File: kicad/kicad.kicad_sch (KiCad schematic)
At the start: 4 parts, among them SW1 SW_Push, U1 nice_nano, U2 GY-BNO08X, U3 SSD1306_OLED_042

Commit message: started working on new pcb
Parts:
- added SW2: SW_Push, Button_Switch_SMD:SW_Push_1P1T_NO_CK_KSC6xxG, symbol Switch:SW_Push
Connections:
- net GND: now also SW2.2
- net at U1.17 (P1.15): now also SW2.1
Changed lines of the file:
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@@
+	(wire
+		(pts
+			(xy 104.14 60.96) (xy 111.76 60.96)
+		)
+		(stroke
+			(width 0)
+			(type default)
+		)
+	)
 	(wire
 		(pts
@@
 	(wire
 		(pts
+			(xy 121.92 58.42) (xy 124.46 58.42)
+		)
+		(stroke
+			(width 0)
+			(type default)
+		)
+	)
+	(wire
+		(pts
 			(xy 68.58 35.56) (xy 68.58 31.75)
 		)
@@
 		(pts
 			(xy 67.31 48.26) (xy 68.58 48.26)
+		)
+		(stroke
+			(width 0)
+			(type default)
+		)
+	)
+	(wire
+		(pts
+			(xy 111.76 60.96) (xy 111.76 58.42)
 		)
 		(stroke
@@
 		)
 		(instances
-			(project ""
+			(project "kicad"
 				(path "/80d6febd-194a-41da-8c93-73e5ad43e615"
 					(reference "U2")
@@
 		)
 		(instances
-			(project ""
+			(project "kicad"
 				(path "/80d6febd-194a-41da-8c93-73e5ad43e615"
 					(reference "#PWR02")
@@
 		)
 		(instances
-			(project ""
+			(project "kicad"
 				(path "/80d6febd-194a-41da-8c93-73e5ad43e615"
 					(reference "#PWR03")
@@
 	(symbol
 		(lib_id "Switch:SW_Push")
+		(at 116.84 58.42 0)
+		(unit 1)
+		(exclude_from_sim no)
+		(in_bom yes)
+		(on_board yes)
+		(dnp no)
+		(fields_autoplaced yes)
+		(property "Reference" "SW2"
+			(at 115.5699 54.61 90)
+			(effects
+				(font
+					(size 1.27 1.27)
+				)
+				(justify left)
+			)
+		)
+		(property "Value" "SW_Push"
+			(at 118.1099 54.61 90)
+			(effects
+				(font
+					(size 1.27 1.27)
+				)
+				(justify left)
+			)
+		)
+		(property "Footprint" "Button_Switch_SMD:SW_Push_1P1T_NO_CK_KSC6xxG"
+			(at 116.84 53.34 0)
+			(effects
+				(font
+					(size 1.27 1.27)
+				)
+				(hide yes)
+			)
+		)
+		(property "Datasheet" "~"
+			(at 116.84 53.34 0)
+			(effects
+				(font
+					(size 1.27 1.27)
+				)
+				(hide yes)
+			)
+		)
+		(property "Description" "Push button switch, generic, two pins"
+			(at 116.84 58.42 0)
+			(effects
+				(font
+					(size 1.27 1.27)
+				)
+				(hide yes)
+			)
+		)
+		(pin "2"
+		)
+		(pin "1"
+		)
+		(instances
+			(project "kicad"
+				(path "/80d6febd-194a-41da-8c93-73e5ad43e615"
+					(reference "SW2")
+					(unit 1)
+				)
+			)
+		)
+	)
+	(symbol
+		(lib_id "Switch:SW_Push")
 		(at 116.84 66.04 0)
 		(unit 1)
@@
 		)
 		(instances
-			(project ""
+			(project "kicad"
 				(path "/80d6febd-194a-41da-8c93-73e5ad43e615"
 					(reference "SW1")
@@
 	(symbol
 		(lib_id "power:GND")
+		(at 124.46 58.42 90)
+		(unit 1)
+		(exclude_from_sim no)
+		(in_bom yes)
+		(on_board yes)
+		(dnp no)
+		(fields_autoplaced yes)
+		(property "Reference" "#PWR07"
+			(at 130.81 58.42 0)
+			(effects
+				(font
+					(size 1.27 1.27)
+				)
+				(hide yes)
+			)
+		)
+		(property "Value" "GND"
+			(at 129.54 58.42 0)
+			(effects
+				(font
+					(size 1.27 1.27)
+				)
+			)
+		)
+		(property "Footprint" ""
+			(at 124.46 58.42 0)
+			(effects
+				(font
+					(size 1.27 1.27)
+				)
+				(hide yes)
+			)
+		)
+		(property "Datasheet" ""
+			(at 124.46 58.42 0)
+			(effects
+				(font
+					(size 1.27 1.27)
+				)
+				(hide yes)
+			)
+		)
+		(property "Description" "Power symbol creates a global label with name \"GND\" , ground"
+			(at 124.46 58.42 0)
+			(effects
+				(font
+					(size 1.27 1.27)
+				)
+				(hide yes)
+			)
+		)
+		(pin "1"
+		)
+		(instances
+			(project "kicad"
+				(path "/80d6febd-194a-41da-8c93-73e5ad43e615"
+					(reference "#PWR07")
+					(unit 1)
+				)
+			)
+		)
+	)
+	(symbol
+		(lib_id "power:GND")
 		(at 67.31 48.26 270)
 		(unit 1)
@@
 		)
 		(instances
-			(project ""
+			(project "kicad"
 				(path "/80d6febd-194a-41da-8c93-73e5ad43e615"
 					(reference "U3")
@@
 		)
 		(instances
-			(project ""
+			(project "kicad"
 				(path "/80d6febd-194a-41da-8c93-73e5ad43e615"
 					(reference "#PWR01")
@@
 		)
 		(instances
-			(project ""
+			(project "kicad"
 				(path "/80d6febd-194a-41da-8c93-73e5ad43e615"
 					(reference "U1")

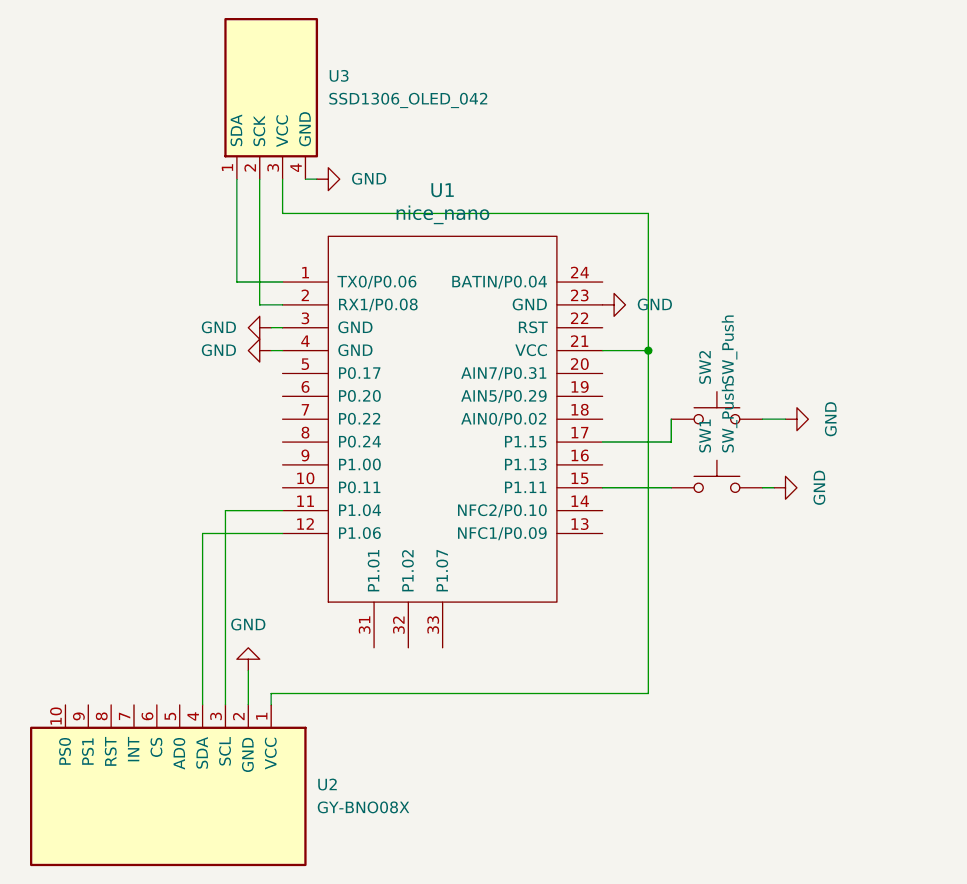
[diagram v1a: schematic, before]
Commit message: add b+ and b- pins
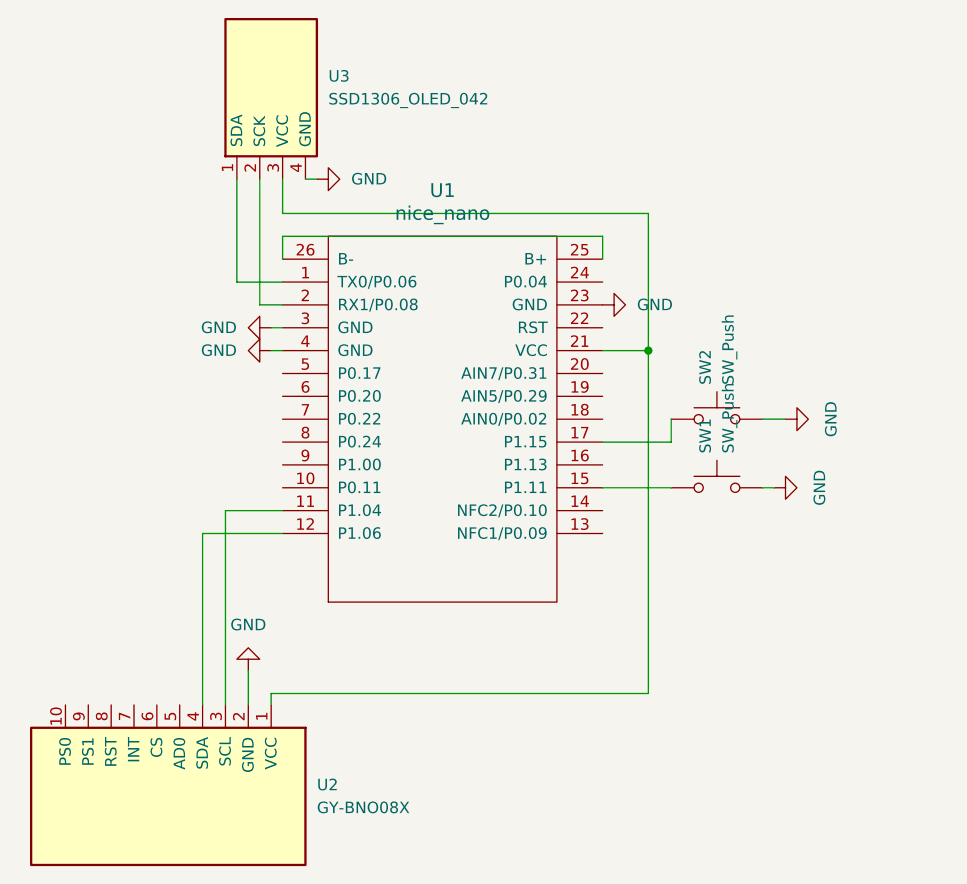
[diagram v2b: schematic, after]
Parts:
- removed U1: nice_nano, nice_nano:nice_nano, symbol nice_nano:nice_nano
- added U1: nice_nano, nice_nano:nice_nano_with_bat_pins, symbol nice-nano:nice_nano_with_bat_pins
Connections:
- net GND: now also U1.23 (GND), U1.3 (GND), U1.4 (GND)
- net at U2.1 (VCC), U3.3 (VCC): now also U1.21 (VCC)
- net at U2.3 (SCL): now also U1.11 (P1.04)
- net at U2.4 (SDA): now also U1.12 (P1.06)
- net at SW2.1: now also U1.17 (P1.15)
- net at SW1.1: now also U1.15 (P1.11)
- net at U3.1 (SDA): now also U1.1 (TX0/P0.06)
- net at U3.2 (SCK): now also U1.2 (RX1/P0.08)
- new net: U1.25 (B+), U1.26 (B-)
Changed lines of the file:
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@@
+	(wire
+		(pts
+			(xy 104.14 38.1) (xy 68.58 38.1)
+		)
+		(stroke
+			(width 0)
+			(type default)
+		)
+	)
 	(wire
 		(pts
@@
 	(wire
 		(pts
+			(xy 104.14 40.64) (xy 104.14 38.1)
+		)
+		(stroke
+			(width 0)
+			(type default)
+		)
+	)
+	(wire
+		(pts
 			(xy 59.69 71.12) (xy 68.58 71.12)
+		)
+		(stroke
+			(width 0)
+			(type default)
+		)
+	)
+	(wire
+		(pts
+			(xy 68.58 38.1) (xy 68.58 40.64)
 		)
 		(stroke
@@
 	)
 	(symbol
+		(lib_id "nice-nano:nice_nano_with_bat_pins")
+		(at 86.36 57.15 0)
+		(unit 1)
+		(exclude_from_sim no)
+		(in_bom yes)
+		(on_board yes)
+		(dnp no)
+		(fields_autoplaced yes)
+		(property "Reference" "U1"
+			(at 86.36 33.02 0)
+			(effects
+				(font
+					(size 1.524 1.524)
+				)
+			)
+		)
+		(property "Value" "nice_nano"
+			(at 86.36 35.56 0)
+			(effects
+				(font
+					(size 1.524 1.524)
+				)
+			)
+		)
+		(property "Footprint" "nice_nano:nice_nano_with_bat_pins"
+			(at 113.03 120.65 90)
+			(effects
+				(font
+					(size 1.524 1.524)
+				)
+				(hide yes)
+			)
+		)
+		(property "Datasheet" ""
+			(at 113.03 120.65 90)
+			(effects
+				(font
+					(size 1.524 1.524)
+				)
+				(hide yes)
+			)
+		)
+		(property "Description" ""
+			(at 86.36 57.15 0)
+			(effects
+				(font
+					(size 1.27 1.27)
+				)
+				(hide yes)
+			)
+		)
+		(pin "15"
+		)
+		(pin "19"
+		)
+		(pin "7"
+		)
+		(pin "17"
+		)
+		(pin "10"
+		)
+		(pin "22"
+		)
+		(pin "8"
+		)
+		(pin "18"
+		)
+		(pin "9"
+		)
+		(pin "11"
+		)
+		(pin "12"
+		)
+		(pin "13"
+		)
+		(pin "16"
+		)
+		(pin "24"
+		)
+		(pin "14"
+		)
+		(pin "2"
+		)
+		(pin "1"
+		)
+		(pin "4"
+		)
+		(pin "3"
+		)
+		(pin "26"
+		)
+		(pin "5"
+		)
+		(pin "6"
+		)
+		(pin "25"
+		)
+		(pin "21"
+		)
+		(pin "20"
+		)
+		(pin "23"
+		)
+		(instances
+			(project "kicad"
+				(path "/80d6febd-194a-41da-8c93-73e5ad43e615"
+					(reference "U1")
+					(unit 1)
+				)
+			)
+		)
+	)
+	(symbol
 		(lib_id "knife_level:SSD1306_OLED_042")
 		(at 67.31 21.59 90)
@@
 					(unit 1)
 				)
-			)
-		)
-	)
-	(symbol
-		(lib_id "nice_nano:nice_nano")
-		(at 86.36 57.15 0)
-		(unit 1)
-		(exclude_from_sim no)
-		(in_bom yes)
-		(on_board yes)
-		(dnp no)
-		(fields_autoplaced yes)
-		(property "Reference" "U1"
-			(at 86.36 33.02 0)
-			(effects
-				(font
-					(size 1.524 1.524)
-				)
-			)
-		)
-		(property "Value" "nice_nano"
-			(at 86.36 35.56 0)
-			(effects
-				(font
-					(size 1.524 1.524)
-				)
-			)
-		)
-		(property "Footprint" "nice_nano:nice_nano"
-			(at 113.03 120.65 90)
-			(effects
-				(font
-					(size 1.524 1.524)
-				)
-				(hide yes)
-			)
-		)
-		(property "Datasheet" ""
-			(at 113.03 120.65 90)
-			(effects
-				(font
-					(size 1.524 1.524)
-				)
-				(hide yes)
-			)
-		)
-		(property "Description" ""
-			(at 86.36 57.15 0)
-			(effects
-				(font
-					(size 1.27 1.27)
-				)
-				(hide yes)
-			)
-		)
-		(pin "24"
-		)
-		(pin "21"
-		)
-		(pin "13"
-		)
-		(pin "12"
-		)
-		(pin "33"
-		)
-		(pin "31"
-		)
-		(pin "11"
-		)
-		(pin "15"
-		)
-		(pin "20"
-		)
-		(pin "9"
-		)
-		(pin "10"
-		)
-		(pin "8"
-		)
-		(pin "3"
-		)
-		(pin "2"
-		)
-		(pin "1"
-		)
-		(pin "19"
-		)
-		(pin "17"
-		)
-		(pin "16"
-		)
-		(pin "18"
-		)
-		(pin "22"
-		)
-		(pin "14"
-		)
-		(pin "7"
-		)
-		(pin "6"
-		)
-		(pin "4"
-		)
-		(pin "5"
-		)
-		(pin "23"
-		)
-		(pin "32"
-		)
-		(instances
-			(project "kicad"
-				(path "/80d6febd-194a-41da-8c93-73e5ad43e615"
-					(reference "U1")
-					(unit 1)
-				)

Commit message: fix b+ and b- traces in pcb
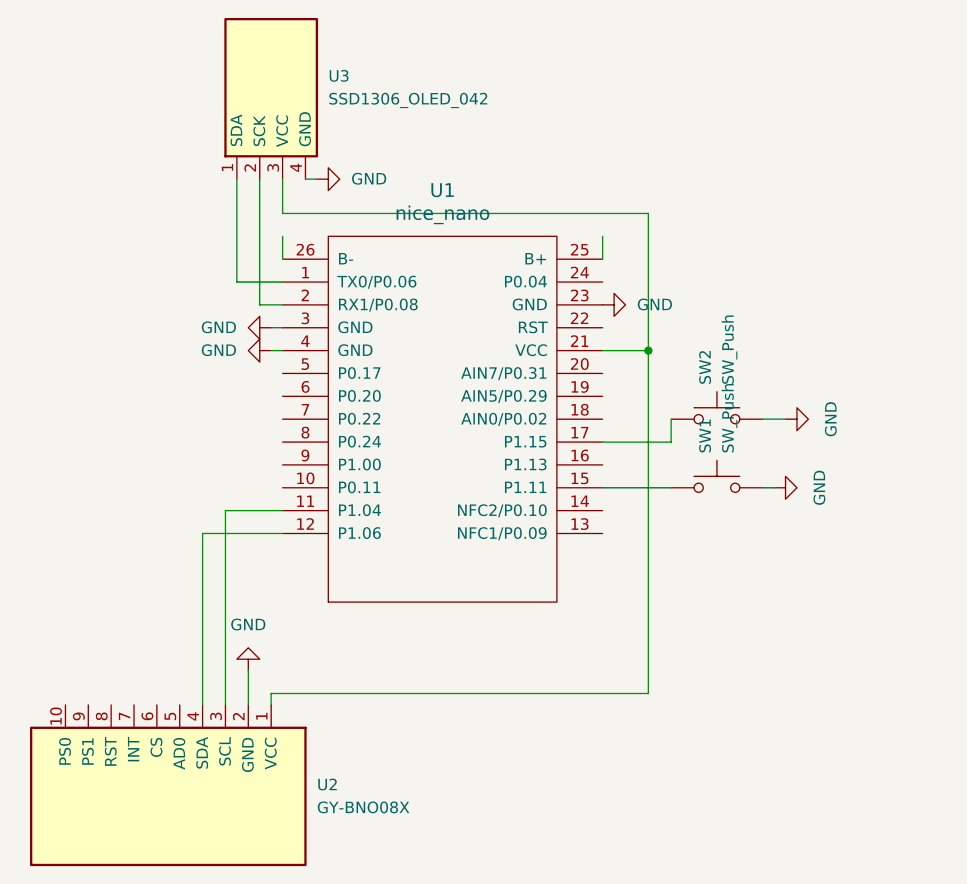
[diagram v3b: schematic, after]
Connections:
- net at U1.25 (B+): no longer U1.26 (B-)
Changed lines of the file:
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@@
-	(wire
-		(pts
-			(xy 104.14 38.1) (xy 68.58 38.1)
-		)
-		(stroke
-			(width 0)
-			(type default)
-		)
-	)
 	(wire
 		(pts

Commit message: kicad cleanup
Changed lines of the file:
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@@
-	(wire
-		(pts
-			(xy 104.14 40.64) (xy 104.14 38.1)
-		)
-		(stroke
-			(width 0)
-			(type default)
-		)
-	)
 	(wire
 		(pts
@@
 		)
 		(stroke
-			(width 0)
-			(type default)
-		)
-	)
-	(wire
-		(pts
-			(xy 68.58 38.1) (xy 68.58 40.64)
-		)
-		(stroke

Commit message: add switch to pcb
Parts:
- added BAT+1, BAT-1: Conn_01x01, Connector_Wire:SolderWire-0.1sqmm_1x01_D0.4mm_OD1mm, symbol Connector_Generic:Conn_01x01
- added SW_POWER1: SW_SPDT, Button_Switch_SMD:SW_SPDT_Shouhan_MSK12C02, symbol Switch:SW_SPDT
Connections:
- net at U1.25 (B+): now also SW_POWER1.2 (B)
- net at U1.26 (B-): now also BAT-1.1 (Pin_1)
- new net: BAT+1.1 (Pin_1), SW_POWER1.3 (C)
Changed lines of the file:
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@@
+	(wire
+		(pts
+			(xy 50.8 40.64) (xy 68.58 40.64)
+		)
+		(stroke
+			(width 0)
+			(type default)
+		)
+	)
 	(wire
 		(pts
@@
 		(pts
 			(xy 59.69 90.17) (xy 59.69 71.12)
+		)
+		(stroke
+			(width 0)
+			(type default)
+		)
+	)
+	(wire
+		(pts
+			(xy 104.14 40.64) (xy 111.76 40.64)
 		)
 		(stroke
@@
 	)
 	(symbol
+		(lib_id "Connector_Generic:Conn_01x01")
+		(at 45.72 40.64 180)
+		(unit 1)
+		(exclude_from_sim no)
+		(in_bom yes)
+		(on_board yes)
+		(dnp no)
+		(fields_autoplaced yes)
+		(property "Reference" "BAT-1"
+			(at 45.72 34.29 0)
+			(effects
+				(font
+					(size 1.27 1.27)
+				)
+			)
+		)
+		(property "Value" "Conn_01x01"
+			(at 45.72 36.83 0)
+			(effects
+				(font
+					(size 1.27 1.27)
+				)
+			)
+		)
+		(property "Footprint" "Connector_Wire:SolderWire-0.1sqmm_1x01_D0.4mm_OD1mm"
+			(at 45.72 40.64 0)
+			(effects
+				(font
+					(size 1.27 1.27)
+				)
+				(hide yes)
+			)
+		)
+		(property "Datasheet" "~"
+			(at 45.72 40.64 0)
+			(effects
+				(font
+					(size 1.27 1.27)
+				)
+				(hide yes)
+			)
+		)
+		(property "Description" "Generic connector, single row, 01x01, script generated (kicad-library-utils/schlib/autogen/connector/)"
+			(at 45.72 40.64 0)
+			(effects
+				(font
+					(size 1.27 1.27)
+				)
+				(hide yes)
+			)
+		)
+		(pin "1"
+		)
+		(instances
+			(project "kicad"
+				(path "/80d6febd-194a-41da-8c93-73e5ad43e615"
+					(reference "BAT-1")
+					(unit 1)
+				)
+			)
+		)
+	)
+	(symbol
 		(lib_id "power:GND")
 		(at 124.46 58.42 90)
@@
 	)
 	(symbol
+		(lib_id "Switch:SW_SPDT")
+		(at 116.84 40.64 0)
+		(unit 1)
+		(exclude_from_sim no)
+		(in_bom yes)
+		(on_board yes)
+		(dnp no)
+		(fields_autoplaced yes)
+		(property "Reference" "SW_POWER1"
+			(at 116.84 31.75 0)
+			(effects
+				(font
+					(size 1.27 1.27)
+				)
+			)
+		)
+		(property "Value" "SW_SPDT"
+			(at 116.84 34.29 0)
+			(effects
+				(font
+					(size 1.27 1.27)
+				)
+			)
+		)
+		(property "Footprint" "Button_Switch_SMD:SW_SPDT_Shouhan_MSK12C02"
+			(at 116.84 40.64 0)
+			(effects
+				(font
+					(size 1.27 1.27)
+				)
+				(hide yes)
+			)
+		)
+		(property "Datasheet" "~"
+			(at 116.84 48.26 0)
+			(effects
+				(font
+					(size 1.27 1.27)
+				)
+				(hide yes)
+			)
+		)
+		(property "Description" "Switch, single pole double throw"
+			(at 116.84 40.64 0)
+			(effects
+				(font
+					(size 1.27 1.27)
+				)
+				(hide yes)
+			)
+		)
+		(pin "2"
+		)
+		(pin "1"
+		)
+		(pin "3"
+		)
+		(instances
+			(project "kicad"
+				(path "/80d6febd-194a-41da-8c93-73e5ad43e615"
+					(reference "SW_POWER1")
+					(unit 1)
+				)
+			)
+		)
+	)
+	(symbol
 		(lib_id "power:GND")
 		(at 123.19 66.04 90)
@@
 					(unit 1)
 				)
+			)
+		)
+	)
+	(symbol
+		(lib_id "Connector_Generic:Conn_01x01")
+		(at 127 43.18 0)
+		(unit 1)
+		(exclude_from_sim no)
+		(in_bom yes)
+		(on_board yes)
+		(dnp no)
+		(fields_autoplaced yes)
+		(property "Reference" "BAT+1"
+			(at 129.54 41.9099 0)
+			(effects
+				(font
+					(size 1.27 1.27)
+				)
+				(justify left)
+			)
+		)
+		(property "Value" "Conn_01x01"
+			(at 129.54 44.4499 0)
+			(effects
+				(font
+					(size 1.27 1.27)
+				)
+				(justify left)
+			)
+		)
+		(property "Footprint" "Connector_Wire:SolderWire-0.1sqmm_1x01_D0.4mm_OD1mm"
+			(at 127 43.18 0)
+			(effects
+				(font
+					(size 1.27 1.27)
+				)
+				(hide yes)
+			)
+		)
+		(property "Datasheet" "~"
+			(at 127 43.18 0)
+			(effects
+				(font
+					(size 1.27 1.27)
+				)
+				(hide yes)
+			)
+		)
+		(property "Description" "Generic connector, single row, 01x01, script generated (kicad-library-utils/schlib/autogen/connector/)"
+			(at 127 43.18 0)
+			(effects
+				(font
+					(size 1.27 1.27)
+				)
+				(hide yes)
+			)
+		)
+		(pin "1"
+		)
+		(instances
+			(project "kicad"
+				(path "/80d6febd-194a-41da-8c93-73e5ad43e615"
+					(reference "BAT+1")
+					(unit 1)
+				)

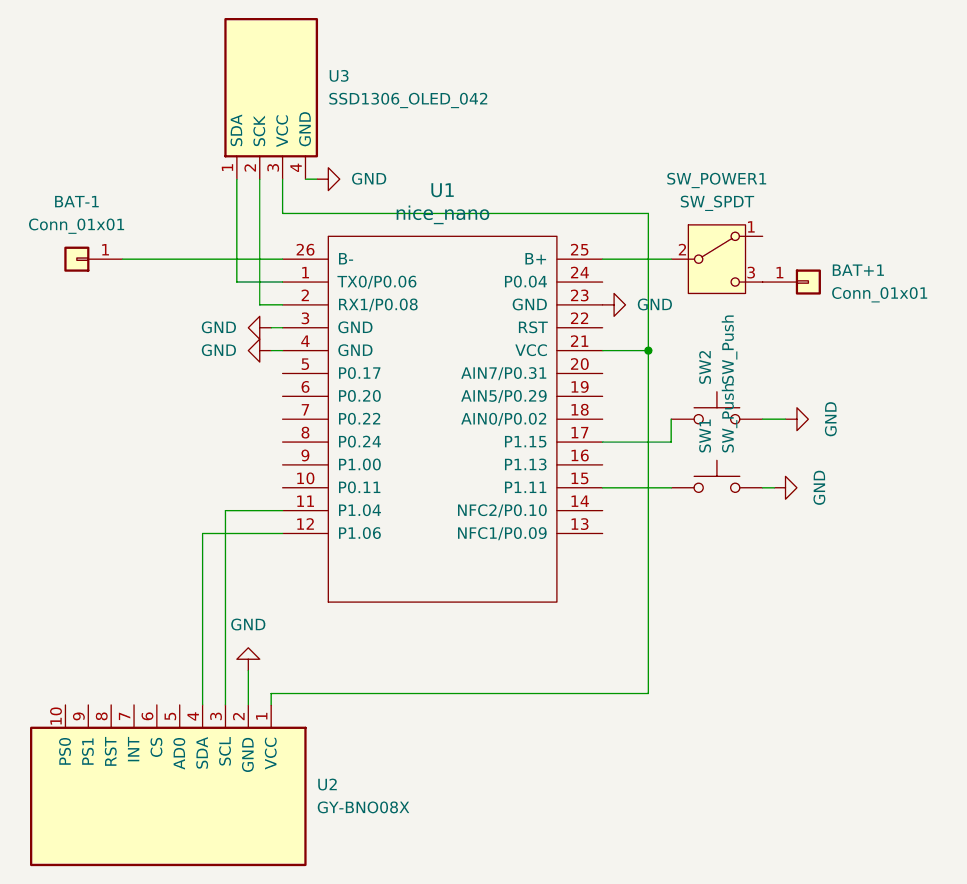
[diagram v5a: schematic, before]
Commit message: move 2nd button to 113
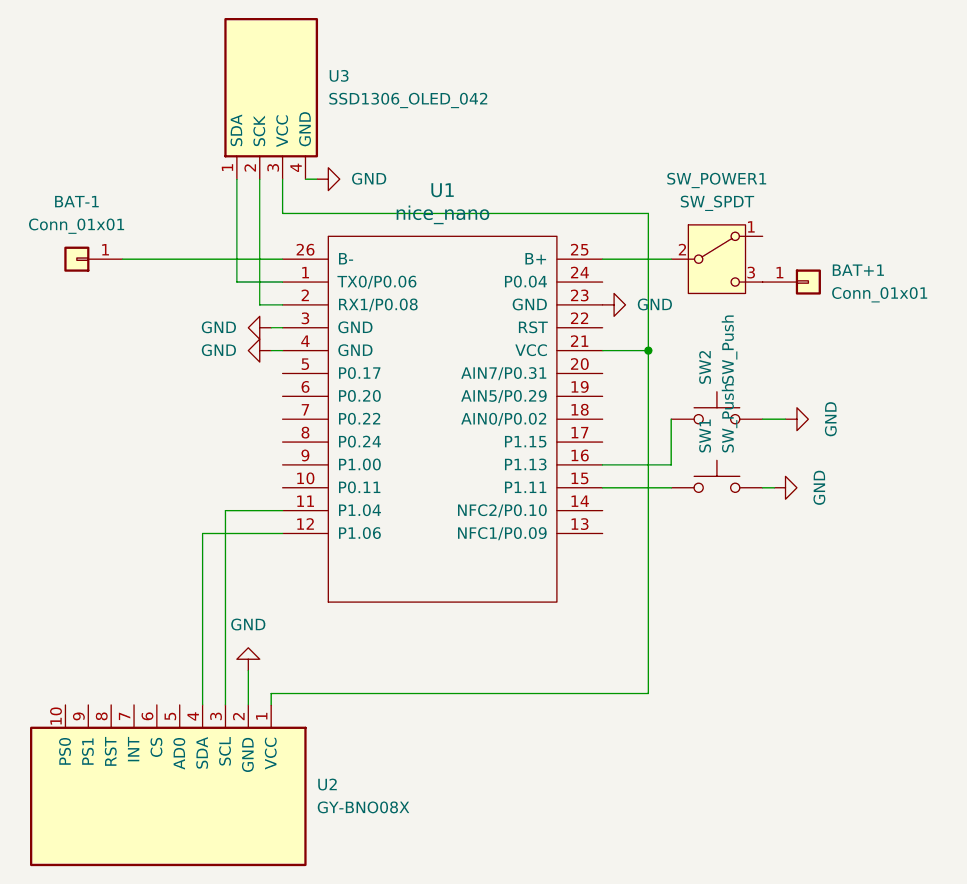
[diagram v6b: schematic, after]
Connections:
- net at SW2.1: now also U1.16 (P1.13); no longer U1.17 (P1.15)
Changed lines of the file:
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@@
-	(wire
-		(pts
-			(xy 104.14 60.96) (xy 111.76 60.96)
-		)
-		(stroke
-			(width 0)
-			(type default)
-		)
-	)
 	(wire
 		(pts
@@
 	(wire
 		(pts
-			(xy 111.76 60.96) (xy 111.76 58.42)
+			(xy 111.76 58.42) (xy 111.76 63.5)
 		)
 		(stroke
@@
 		)
 		(stroke
+			(width 0)
+			(type default)
+		)
+	)
+	(wire
+		(pts
+			(xy 111.76 63.5) (xy 104.14 63.5)
+		)
+		(stroke
